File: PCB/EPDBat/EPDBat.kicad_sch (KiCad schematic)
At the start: 53 parts, among them J1 Conn_01x26, J2 Shelly, J3 JST-PH-SM3-TBT, J3 USB-PROG, J7 USB-C-Socket-V, Q1 BSS138, Q1 C179347, Q4 CJ2301, U2 ESP32-S3-MINI-1, U2 ME6211C33M5G-N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

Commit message: Tracked
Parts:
- removed Q1: C179347, RevK:SOT-323_SC-70, symbol Device:Q_PMOS_GSD
- removed R1: 10K, RevK:R_0402, symbol Device:R
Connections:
- net PWR is gone; now on net VBUS: D4.2 (A), Q4.1 (G), R14.1
- net GND: now also U2.20 (GPIO16)
- net STAT: now also U2.14 (GPIO10); no longer U2.5 (GPIO1)
- net VBAT: now also R12.1
- net ADCFET: no longer names the net of U2.31 (GPIO35)
- net EPDPWR renamed EPDP
- no-connect marks 26 -> 25
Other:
- moved on the sheet: R12, R13

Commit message: BTN added
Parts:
- added J4: Conn_01x02, RevK:PinHeader_1x02_P2.54mm_Vertical, symbol Connector_Generic:Conn_01x02
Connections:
- net GND: now also J4.1 (Pin_1)
- net RGB: now also U2.31 (GPIO35); no longer U2.32 (GPIO36)
- net at R1.1: now also JP1.3 (B); no longer JP1.1 (A)
- net at R1.2: now also JP1.1 (A); no longer JP1.3 (B)
- new net BTN: J4.2 (Pin_2), U2.32 (GPIO36)
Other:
- moved on the sheet: C12, D4, J3, J7, Q1, Q4, R1, R12, R13, R14, R15, R2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

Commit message: As ordered
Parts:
- J3: value JST-PH-SM3-TBT -> JST-PH-SM3-TB; footprint Connector_JST:JST_PH_B2B-PH-SM4-TB_1x02-1MP_P2.00mm_Vertical -> Connector_JST:JST_PH_S2B-PH-SM4-TB_1x02-1MP_P2.00mm_Horizontal; LCSC Part # C265003 -> C295747
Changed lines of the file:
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@@
       (effects (font (size 1.27 1.27)))
     )
-    (property "Value" "JST-PH-SM3-TBT" (at 103.505 24.765 0)
+    (property "Value" "JST-PH-SM3-TB" (at 103.505 24.765 0)
       (effects (font (size 1.27 1.27)))
     )
-    (property "Footprint" "Connector_JST:JST_PH_B2B-PH-SM4-TB_1x02-1MP_P2.00mm_Vertical" (at 104.14 30.48 0)
+    (property "Footprint" "Connector_JST:JST_PH_S2B-PH-SM4-TB_1x02-1MP_P2.00mm_Horizontal" (at 104.14 30.48 0)
       (effects (font (size 1.27 1.27)) hide)
     )
@@
       (effects (font (size 1.27 1.27)) hide)
     )
-    (property "LCSC Part #" "C265003" (at 104.14 30.48 0)
+    (property "LCSC Part #" "C295747" (at 104.14 30.48 0)
       (effects (font (size 1.27 1.27)) hide)
     )

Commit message: ESD
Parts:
- removed U5: TP4054, RevK:SOT-23-5, symbol Watchy-rescue:MCP73831-2-OT-Battery_Management
- added D6: ~, RevK:DFN1006-2L, symbol RevK:ES05D1MC10
- added U1: TP4054, RevK:SOT-23-5, symbol RevK:TP4054
- D1, D2, D3: footprint RevK:D_SOD-123 -> Diode_THT:D_DO-41_SOD81_P10.16mm_Horizontal
- Q1, Q4: footprint RevK:SOT-23 -> Package_TO_SOT_SMD:SOT-23
- U2: footprint RevK:SOT-23-5 -> Package_TO_SOT_SMD:SOT-23-5
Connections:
- net BTN: now also D6.1
- net GND: now also D6.2, U1.2 (VSS)
- net STAT: now also U1.1 (STAT)
- net VBAT: now also U1.3 (VBAT)
- net VBUS: now also U1.4 (VDD)
- net at R15.2: now also U1.5 (PROG)
- net +3V3 renamed +3.3V
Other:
- moved on the sheet: R15

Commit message: ESD
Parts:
- removed D1, D2, D3: MBR0530, Diode_THT:D_DO-41_SOD81_P10.16mm_Horizontal, symbol Diode:1N5819
- added D4 (x3): MBR0530, RevK:D_SOD-123, symbol Device:D_Schottky
- D4: LCSC Part  (none) -> C5204746
- Q1, Q4: footprint Package_TO_SOT_SMD:SOT-23 -> RevK:SOT-23
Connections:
- net BTN: now also D6.2; no longer D6.1
- net GND: now also D6.1, D4.1 (K); no longer D6.2
- net at C3.1, L1.1, Q1.3 (D): now also D4.2 (A)
- net at C3.1, J1.21 (Pin_21): now also D4.1 (K)
- net at C3.2: now also D4.1 (K), D4.2 (A)
- net at C3.1, J1.23 (Pin_23): now also D4.2 (A)
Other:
- moved on the sheet: D6
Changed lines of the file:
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@@
   (junction (at 187.96 100.33) (diameter 0) (color 0 0 0 0)
   )
+  (junction (at 98.425 56.515) (diameter 0) (color 0 0 0 0)
+  )
   (junction (at 87.63 102.235) (diameter 0) (color 0 0 0 0)
   )
@@
   )
   (junction (at 161.29 124.46) (diameter 0) (color 0 0 0 0)
-  )
-  (junction (at 98.425 56.515) (diameter 0) (color 0 0 0 0)
   )
   (junction (at 161.29 104.775) (diameter 0) (color 0 0 0 0)
@@
       (effects (font (size 1.27 1.27)) (justify left))
     )
-    (property "Footprint" "Package_TO_SOT_SMD:SOT-23" (at 182.245 142.875 0)
+    (property "Footprint" "RevK:SOT-23" (at 182.245 142.875 0)
       (effects (font (size 1.27 1.27) italic) (justify left) hide)
     )
@@
       (effects (font (size 1.27 1.27)) (justify left))
     )
-    (property "Footprint" "Package_TO_SOT_SMD:SOT-23" (at 159.385 25.4 0)
+    (property "Footprint" "RevK:SOT-23" (at 159.385 25.4 0)
       (effects (font (size 1.27 1.27) italic) (justify left) hide)
     )
@@
     )
   )
-  (symbol (lib_id "RevK:ES05D1MC10") (at 98.425 62.865 90) (unit 1)
+  (symbol (lib_id "RevK:ES05D1MC10") (at 98.425 62.865 270) (unit 1)
     (in_bom yes) (on_board yes) (dnp no) (fields_autoplaced)
     (property "Reference" "D6" (at 100.457 62.865 90)
-      (effects (font (size 1.27 1.27)) (justify right))
+      (effects (font (size 1.27 1.27)) (justify left))
     )
     (property "Value" "~" (at 98.425 62.865 0)
       (effects (font (size 1.27 1.27)))
     )
-    (property "Footprint" "RevK:DFN1006-2L" (at 95.25 62.23 0)
+    (property "Footprint" "RevK:DFN1006-2L" (at 101.6 63.5 0)
       (effects (font (size 1.27 1.27)) hide)
     )
@@
       (effects (font (size 1.27 1.27)) hide)
     )
-    (property "LCSC Part #" "C5137770" (at 101.6 62.865 0)
+    (property "LCSC Part #" "C5137770" (at 95.25 62.865 0)
       (effects (font (size 1.27 1.27)) hide)
     )
@@
         (path "/46c350bb-7de4-4e81-aafd-4af55e37aab0"
           (reference "D6") (unit 1)
+        )
+      )
+    )
+  )
+  (symbol (lib_id "Device:D_Schottky") (at 180.34 69.85 0) (unit 1)
+    (in_bom yes) (on_board yes) (dnp no)
+    (property "Reference" "D4" (at 183.515 68.58 0)
+      (effects (font (size 1.27 1.27)))
+    )
+    (property "Value" "MBR0530" (at 173.355 68.58 0)
+      (effects (font (size 1.27 1.27)))
+    )
+    (property "Footprint" "RevK:D_SOD-123" (at 180.34 69.85 0)
+      (effects (font (size 1.27 1.27)) hide)
+    )
+    (property "Datasheet" "~" (at 180.34 69.85 0)
+      (effects (font (size 1.27 1.27)) hide)
+    )
+    (property "LCSC Part " "C5204746" (at 180.34 69.85 0)
+      (effects (font (size 1.27 1.27)) hide)
+    )
+    (pin "1")
+    (pin "2")
+    (instances
+      (project "Watchy"
+        (path "/03039abc-65dd-445c-a352-9e386e1f31aa"
+          (reference "D4") (unit 1)
+        )
+      )
+      (project "EPDBat"
+        (path "/46c350bb-7de4-4e81-aafd-4af55e37aab0"
+          (reference "D1") (unit 1)
         )
       )
@@
     )
   )
-  (symbol (lib_id "Diode:1N5819") (at 180.34 85.09 0) (unit 1)
-    (in_bom yes) (on_board yes) (dnp no)
-    (property "Reference" "D3" (at 176.53 83.82 0)
-      (effects (font (size 1.27 1.27)))
-    )
-    (property "Value" "MBR0530" (at 173.355 86.36 0)
-      (effects (font (size 1.27 1.27)))
-    )
-    (property "Footprint" "Diode_THT:D_DO-41_SOD81_P10.16mm_Horizontal" (at 180.34 89.535 0)
-      (effects (font (size 1.27 1.27)) hide)
-    )
-    (property "Datasheet" "http://www.vishay.com/docs/88525/1n5817.pdf" (at 180.34 85.09 0)
-      (effects (font (size 1.27 1.27)) hide)
-    )
-    (property "LCSC Part #" "C5204746" (at 180.34 85.09 0)
-      (effects (font (size 1.27 1.27)) hide)
-    )
-    (pin "1")
-    (pin "2")
-    (instances
-      (project "EPDBat"
-        (path "/46c350bb-7de4-4e81-aafd-4af55e37aab0"
-          (reference "D3") (unit 1)
-        )
-      )
-    )
-  )
   (symbol (lib_id "power:GND") (at 157.48 43.18 0) (unit 1)
     (in_bom yes) (on_board yes) (dnp no)
@@
     )
   )
-  (symbol (lib_id "Diode:1N5819") (at 180.34 77.47 180) (unit 1)
-    (in_bom yes) (on_board yes) (dnp no)
-    (property "Reference" "D2" (at 177.165 76.2 0)
-      (effects (font (size 1.27 1.27)))
-    )
-    (property "Value" "MBR0530" (at 173.99 78.74 0)
-      (effects (font (size 1.27 1.27)))
-    )
-    (property "Footprint" "Diode_THT:D_DO-41_SOD81_P10.16mm_Horizontal" (at 180.34 73.025 0)
-      (effects (font (size 1.27 1.27)) hide)
-    )
-    (property "Datasheet" "http://www.vishay.com/docs/88525/1n5817.pdf" (at 180.34 77.47 0)
-      (effects (font (size 1.27 1.27)) hide)
-    )
-    (property "LCSC Part #" "C5204746" (at 180.34 77.47 0)
-      (effects (font (size 1.27 1.27)) hide)
-    )
-    (pin "1")
-    (pin "2")
-    (instances
-      (project "EPDBat"
-        (path "/46c350bb-7de4-4e81-aafd-4af55e37aab0"
-          (reference "D2") (unit 1)
-        )
-      )
-    )
-  )
   (symbol (lib_id "power:+3.3V") (at 229.235 22.86 0) (unit 1)
     (in_bom yes) (on_board yes) (dnp no) (fields_autoplaced)
@@
         (path "/46c350bb-7de4-4e81-aafd-4af55e37aab0"
           (reference "JP2") (unit 1)
+        )
+      )
+    )
+  )
+  (symbol (lib_id "Device:D_Schottky") (at 180.34 77.47 180) (unit 1)
+    (in_bom yes) (on_board yes) (dnp no)
+    (property "Reference" "D4" (at 183.515 76.2 0)
+      (effects (font (size 1.27 1.27)))
+    )
+    (property "Value" "MBR0530" (at 174.625 76.2 0)
+      (effects (font (size 1.27 1.27)))
+    )
+    (property "Footprint" "RevK:D_SOD-123" (at 180.34 77.47 0)
+      (effects (font (size 1.27 1.27)) hide)
+    )
+    (property "Datasheet" "~" (at 180.34 77.47 0)
+      (effects (font (size 1.27 1.27)) hide)
+    )
+    (property "LCSC Part " "C5204746" (at 180.34 77.47 0)
+      (effects (font (size 1.27 1.27)) hide)
+    )
+    (pin "1")
+    (pin "2")
+    (instances
+      (project "Watchy"
+        (path "/03039abc-65dd-445c-a352-9e386e1f31aa"
+          (reference "D4") (unit 1)
+        )
+      )
+      (project "EPDBat"
+        (path "/46c350bb-7de4-4e81-aafd-4af55e37aab0"
+          (reference "D2") (unit 1)
         )
       )
@@
       (effects (font (size 1.27 1.27)) hide)
     )
+    (property "LCSC Part " "C5204746" (at 166.37 35.56 0)
+      (effects (font (size 1.27 1.27)) hide)
+    )
     (pin "1")
     (pin "2")
@@
         (path "/46c350bb-7de4-4e81-aafd-4af55e37aab0"
           (reference "C11") (unit 1)
-        )
-      )
-    )
-  )
-  (symbol (lib_id "Diode:1N5819") (at 180.34 69.85 0) (unit 1)
-    (in_bom yes) (on_board yes) (dnp no)
-    (property "Reference" "D1" (at 176.53 68.58 0)
-      (effects (font (size 1.27 1.27)))
-    )
-    (property "Value" "MBR0530" (at 173.355 71.12 0)
-      (effects (font (size 1.27 1.27)))
-    )
-    (property "Footprint" "Diode_THT:D_DO-41_SOD81_P10.16mm_Horizontal" (at 180.34 74.295 0)
-      (effects (font (size 1.27 1.27)) hide)
-    )
-    (property "Datasheet" "http://www.vishay.com/docs/88525/1n5817.pdf" (at 180.34 69.85 0)
-      (effects (font (size 1.27 1.27)) hide)
-    )
-    (property "LCSC Part #" "C5204746" (at 180.34 69.85 0)
-      (effects (font (size 1.27 1.27)) hide)
-    )
-    (pin "1")
-    (pin "2")
-    (instances
-      (project "EPDBat"
-        (path "/46c350bb-7de4-4e81-aafd-4af55e37aab0"
-          (reference "D1") (unit 1)
         )
       )
@@
         )
       )
+    )
+  )
+  (symbol (lib_id "Device:D_Schottky") (at 180.34 85.09 0) (unit 1)
+    (in_bom yes) (on_board yes) (dnp no)
+    (property "Reference" "D4" (at 183.515 83.82 0)
+      (effects (font (size 1.27 1.27)))
+    )
+    (property "Value" "MBR0530" (at 173.355 83.82 0)
+      (effects (font (size 1.27 1.27)))
+    )
+    (property "Footprint" "RevK:D_SOD-123" (at 180.34 85.09 0)
+      (effects (font (size 1.27 1.27)) hide)
+    )
+    (property "Datasheet" "~" (at 180.34 85.09 0)
+      (effects (font (size 1.27 1.27)) hide)
+    )
+    (property "LCSC Part " "C5204746" (at 180.34 85.09 0)
+      (effects (font (size 1.27 1.27)) hide)
+    )
+    (pin "1")
+    (pin "2")
+    (instances
+      (project "Watchy"
+        (path "/03039abc-65dd-445c-a352-9e386e1f31aa"
+          (reference "D4") (unit 1)
+        )
+      )
+      (project "EPDBat"
+        (path "/46c350bb-7de4-4e81-aafd-4af55e37aab0"
+          (reference "D3") (unit 1)
+        )
+      )

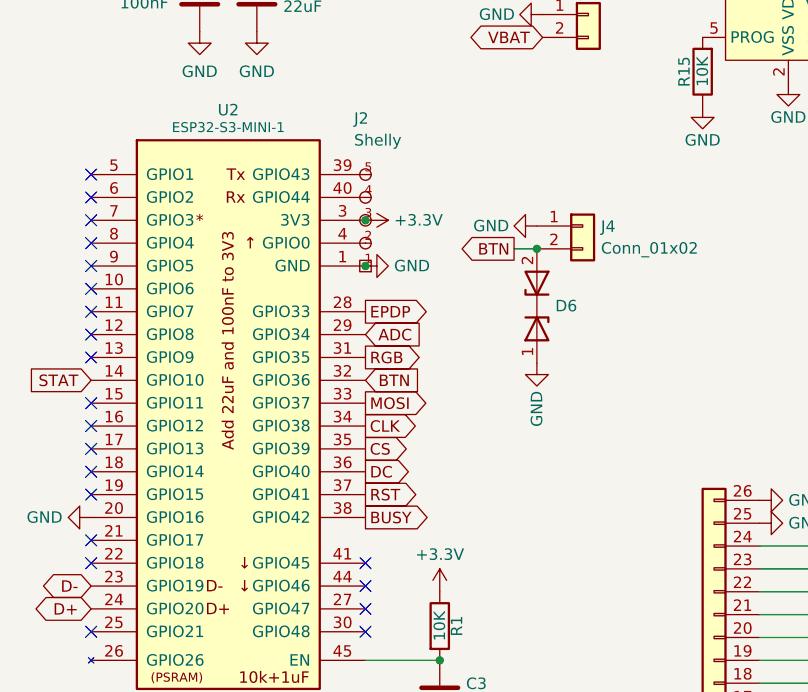
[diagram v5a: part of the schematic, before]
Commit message: Moved connector to reduce slack
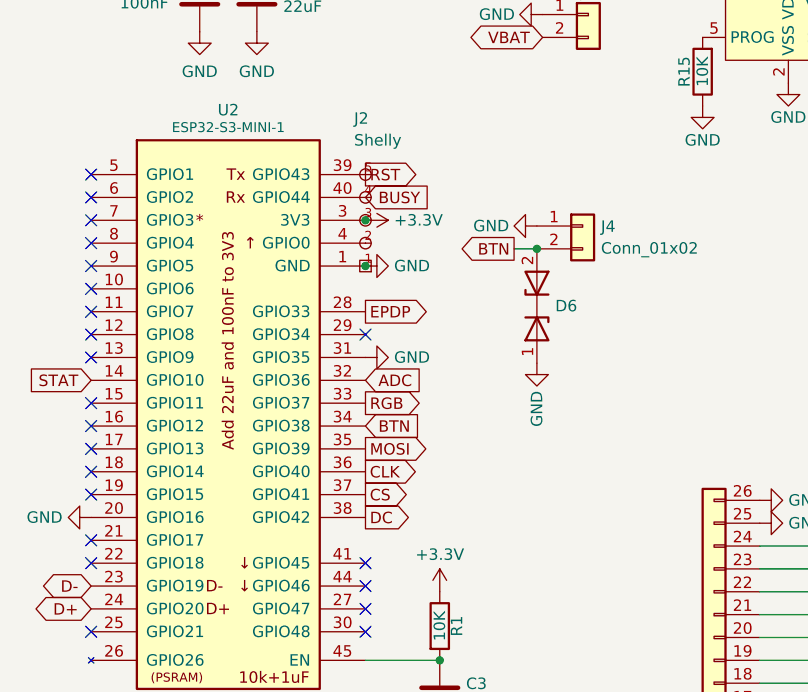
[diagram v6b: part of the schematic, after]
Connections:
- net ADC: now also U2.32 (GPIO36); no longer U2.29 (GPIO34)
- net BTN: now also U2.34 (GPIO38); no longer U2.32 (GPIO36)
- net BUSY: now also J2.4 (Rx), U2.40 (GPIO44); no longer U2.38 (GPIO42)
- net CLK: now also U2.36 (GPIO40); no longer U2.34 (GPIO38)
- net CS: now also U2.37 (GPIO41); no longer U2.35 (GPIO39)
- net DC: now also U2.38 (GPIO42); no longer U2.36 (GPIO40)
- net GND: now also U2.31 (GPIO35)
- net MOSI: now also U2.35 (GPIO39); no longer U2.33 (GPIO37)
- net RGB: now also U2.33 (GPIO37); no longer U2.31 (GPIO35)
- net RST: now also J2.5 (Tx), U2.39 (GPIO43); no longer U2.37 (GPIO41)
- no-connect marks 25 -> 26
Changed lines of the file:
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@@
   (no_connect (at 79.375 91.44))
   (no_connect (at 79.375 99.06))
+  (no_connect (at 79.375 66.04))
   (no_connect (at 48.895 53.34))
   (no_connect (at 48.895 81.28))
@@
     (stroke (width 0) (type default))
   )
-  (global_label "BTN" (shape input) (at 79.375 71.12 0) (fields_autoplaced)
-    (effects (font (size 1.27 1.27)) (justify left))
-    (property "Intersheetrefs" "${INTERSHEET_REFS}" (at 85.2741 71.12 0)
+  (global_label "BTN" (shape input) (at 79.375 76.2 0) (fields_autoplaced)
+    (effects (font (size 1.27 1.27)) (justify left))
+    (property "Intersheetrefs" "${INTERSHEET_REFS}" (at 85.2741 76.2 0)
       (effects (font (size 1.27 1.27)) (justify left) hide)
     )
@@
     )
   )
-  (global_label "MOSI" (shape output) (at 79.375 73.66 0) (fields_autoplaced)
-    (effects (font (size 1.27 1.27)) (justify left))
-    (property "Intersheetrefs" "${INTERSHEET_REFS}" (at 86.3022 73.66 0)
+  (global_label "MOSI" (shape output) (at 79.375 78.74 0) (fields_autoplaced)
+    (effects (font (size 1.27 1.27)) (justify left))
+    (property "Intersheetrefs" "${INTERSHEET_REFS}" (at 86.3022 78.74 0)
       (effects (font (size 1.27 1.27)) (justify left) hide)
     )
@@
     )
   )
-  (global_label "BUSY" (shape output) (at 79.375 86.36 0) (fields_autoplaced)
-    (effects (font (size 1.27 1.27)) (justify left))
-    (property "Intersheetrefs" "${INTERSHEET_REFS}" (at 86.6046 86.36 0)
+  (global_label "BUSY" (shape input) (at 79.375 50.8 0) (fields_autoplaced)
+    (effects (font (size 1.27 1.27)) (justify left))
+    (property "Intersheetrefs" "${INTERSHEET_REFS}" (at 86.6046 50.8 0)
       (effects (font (size 1.27 1.27)) (justify left) hide)
     )
@@
     )
   )
-  (global_label "DC" (shape output) (at 79.375 81.28 0) (fields_autoplaced)
-    (effects (font (size 1.27 1.27)) (justify left))
-    (property "Intersheetrefs" "${INTERSHEET_REFS}" (at 84.246 81.28 0)
+  (global_label "DC" (shape output) (at 79.375 86.36 0) (fields_autoplaced)
+    (effects (font (size 1.27 1.27)) (justify left))
+    (property "Intersheetrefs" "${INTERSHEET_REFS}" (at 84.246 86.36 0)
       (effects (font (size 1.27 1.27)) (justify left) hide)
     )
@@
     )
   )
-  (global_label "RST" (shape output) (at 79.375 83.82 0) (fields_autoplaced)
-    (effects (font (size 1.27 1.27)) (justify left))
-    (property "Intersheetrefs" "${INTERSHEET_REFS}" (at 85.1531 83.82 0)
+  (global_label "RST" (shape output) (at 79.375 48.26 0) (fields_autoplaced)
+    (effects (font (size 1.27 1.27)) (justify left))
+    (property "Intersheetrefs" "${INTERSHEET_REFS}" (at 85.1531 48.26 0)
       (effects (font (size 1.27 1.27)) (justify left) hide)
     )
@@
     )
   )
-  (global_label "CS" (shape output) (at 79.375 78.74 0) (fields_autoplaced)
-    (effects (font (size 1.27 1.27)) (justify left))
-    (property "Intersheetrefs" "${INTERSHEET_REFS}" (at 84.1855 78.74 0)
+  (global_label "CS" (shape output) (at 79.375 83.82 0) (fields_autoplaced)
+    (effects (font (size 1.27 1.27)) (justify left))
+    (property "Intersheetrefs" "${INTERSHEET_REFS}" (at 84.1855 83.82 0)
       (effects (font (size 1.27 1.27)) (justify left) hide)
     )
@@
     )
   )
-  (global_label "RGB" (shape output) (at 79.375 68.58 0) (fields_autoplaced)
-    (effects (font (size 1.27 1.27)) (justify left))
-    (property "Intersheetrefs" "${INTERSHEET_REFS}" (at 85.516 68.58 0)
+  (global_label "RGB" (shape output) (at 79.375 73.66 0) (fields_autoplaced)
+    (effects (font (size 1.27 1.27)) (justify left))
+    (property "Intersheetrefs" "${INTERSHEET_REFS}" (at 85.516 73.66 0)
       (effects (font (size 1.27 1.27)) (justify left) hide)
     )
@@
     )
   )
-  (global_label "CLK" (shape output) (at 79.375 76.2 0) (fields_autoplaced)
-    (effects (font (size 1.27 1.27)) (justify left))
-    (property "Intersheetrefs" "${INTERSHEET_REFS}" (at 85.2741 76.2 0)
+  (global_label "CLK" (shape output) (at 79.375 81.28 0) (fields_autoplaced)
+    (effects (font (size 1.27 1.27)) (justify left))
+    (property "Intersheetrefs" "${INTERSHEET_REFS}" (at 85.2741 81.28 0)
       (effects (font (size 1.27 1.27)) (justify left) hide)
     )
@@
     )
   )
-  (global_label "ADC" (shape input) (at 79.375 66.04 0)
-    (effects (font (size 1.27 1.27)) (justify left))
-    (property "Intersheetrefs" "${INTERSHEET_REFS}" (at 79.375 66.04 0)
+  (global_label "ADC" (shape input) (at 79.375 71.12 0)
+    (effects (font (size 1.27 1.27)) (justify left))
+    (property "Intersheetrefs" "${INTERSHEET_REFS}" (at 79.375 71.12 0)
       (effects (font (size 1.27 1.27)) hide)
     )
@@
         )
       )
+    )
+  )
+  (symbol (lib_id "power:GND") (at 79.375 68.58 90) (unit 1)
+    (in_bom yes) (on_board yes) (dnp no) (fields_autoplaced)
+    (property "Reference" "#PWR01" (at 85.725 68.58 0)
+      (effects (font (size 1.27 1.27)) hide)
+    )
+    (property "Value" "GND" (at 82.55 68.58 90)
+      (effects (font (size 1.27 1.27)) (justify right))
+    )
+    (property "Footprint" "" (at 79.375 68.58 0)
+      (effects (font (size 1.27 1.27)) hide)
+    )
+    (property "Datasheet" "" (at 79.375 68.58 0)
+      (effects (font (size 1.27 1.27)) hide)
+    )
+    (pin "1")
+    (instances
+      (project "USBA"
+        (path "/2d210a96-f81f-42a9-8bf4-1b43c11086f3"
+          (reference "#PWR01") (unit 1)
+        )
+      )
+      (project "EPDBat"
+        (path "/46c350bb-7de4-4e81-aafd-4af55e37aab0"
+          (reference "#PWR025") (unit 1)
+        )
+      )

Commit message: Changed ESD
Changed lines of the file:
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@@
     )
   )
-  (symbol (lib_id "RevK:ES05D1MC10") (at 98.425 62.865 270) (unit 1)
-    (in_bom yes) (on_board yes) (dnp no) (fields_autoplaced)
-    (property "Reference" "D6" (at 100.457 62.865 90)
+  (symbol (lib_id "RevK:ES05D1MC10") (at 98.425 60.325 270) (unit 1)
+    (in_bom yes) (on_board yes) (dnp no) (fields_autoplaced)
+    (property "Reference" "D6" (at 100.457 60.325 90)
       (effects (font (size 1.27 1.27)) (justify left))
     )
-    (property "Value" "~" (at 98.425 62.865 0)
-      (effects (font (size 1.27 1.27)))
-    )
-    (property "Footprint" "RevK:DFN1006-2L" (at 101.6 63.5 0)
-      (effects (font (size 1.27 1.27)) hide)
-    )
-    (property "Datasheet" "" (at 98.425 62.865 0)
-      (effects (font (size 1.27 1.27)) hide)
-    )
-    (property "LCSC Part #" "C5137770" (at 95.25 62.865 0)
+    (property "Value" "~" (at 98.425 60.325 0)
+      (effects (font (size 1.27 1.27)))
+    )
+    (property "Footprint" "RevK:DFN1006-2L" (at 101.6 60.96 0)
+      (effects (font (size 1.27 1.27)) hide)
+    )
+    (property "Datasheet" "" (at 98.425 60.325 0)
+      (effects (font (size 1.27 1.27)) hide)
+    )
+    (property "LCSC Part #" "C5137770" (at 95.25 60.325 0)
       (effects (font (size 1.27 1.27)) hide)
     )
@@
     )
   )
-  (symbol (lib_id "power:GND") (at 98.425 69.215 0) (unit 1)
-    (in_bom yes) (on_board yes) (dnp no)
-    (property "Reference" "#PWR056" (at 98.425 75.565 0)
-      (effects (font (size 1.27 1.27)) hide)
-    )
-    (property "Value" "GND" (at 98.425 74.295 90)
-      (effects (font (size 1.27 1.27)))
-    )
-    (property "Footprint" "" (at 98.425 69.215 0)
-      (effects (font (size 1.27 1.27)) hide)
-    )
-    (property "Datasheet" "" (at 98.425 69.215 0)
-      (effects (font (size 1.27 1.27)) hide)
-    )
+  (symbol (lib_id "power:GND") (at 98.425 64.135 0) (unit 1)
+    (in_bom yes) (on_board yes) (dnp no)
+    (property "Reference" "#PWR056" (at 98.425 70.485 0)
+      (effects (font (size 1.27 1.27)) hide)
+    )
+    (property "Value" "GND" (at 98.425 69.215 90)
+      (effects (font (size 1.27 1.27)))
+    )
+    (property "Footprint" "" (at 98.425 64.135 0)
+      (effects (font (size 1.27 1.27)) hide)
+    )
+    (property "Datasheet" "" (at 98.425 64.135 0)
+      (effects (font (size 1.27 1.27)) hide)
+    )

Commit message: Update for new USB leads
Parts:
- removed J2: Shelly, RevK:Shelly, symbol RevK:Shelly
- removed J3: USB-PROG, RevK:USB-PROG, symbol RevK:USB-PROG
- added J5: TC2030-USB-NL-DS, RevK:Tag-Connect_TC2030-IDC-NL_2x03_P1.27mm_Vertical, symbol RevK:TC2030-USB-NL
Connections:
- net D+: now also J5.4 (D+)
- net D-: now also J5.3 (D-)
- net GND: now also J5.5 (GND), J5.6 (GND)
- net VBUS: now also J5.1 (VBUS), J5.2 (VBUS)
- no-connect marks 26 -> 27
